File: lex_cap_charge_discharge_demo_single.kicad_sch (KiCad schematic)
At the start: 8 parts, among them J1 +5V, J2 GND, SW1 charge, SW2 discharge

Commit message: Put rev. 1.0 on schematic sheet info box
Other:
- note added: "1.0"
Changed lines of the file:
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@@
 	(generator_version "9.0")
 	(paper "A5")
+	(text "1.0"
+		(exclude_from_sim no)
+		(at 184.404 131.318 0)
+		(effects
+			(font
+				(size 1.524 1.524)
+			)
+		)
+	)
 	(text "momentary"
 		(exclude_from_sim no)

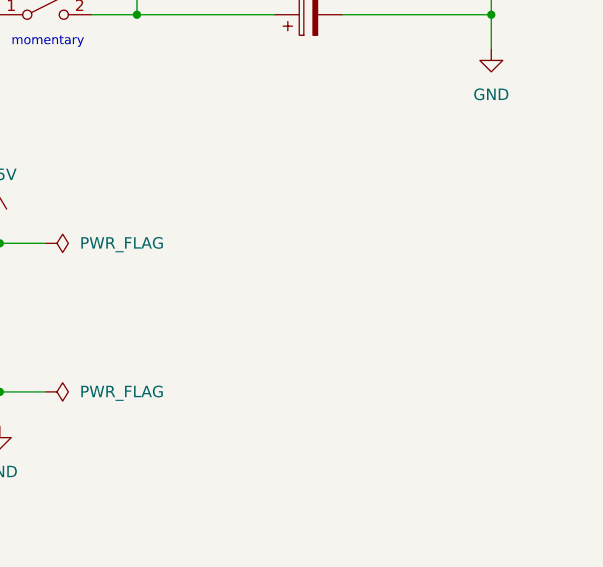
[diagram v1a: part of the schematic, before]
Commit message: Add 2.2mm mounting holes at corners (made board bigger)
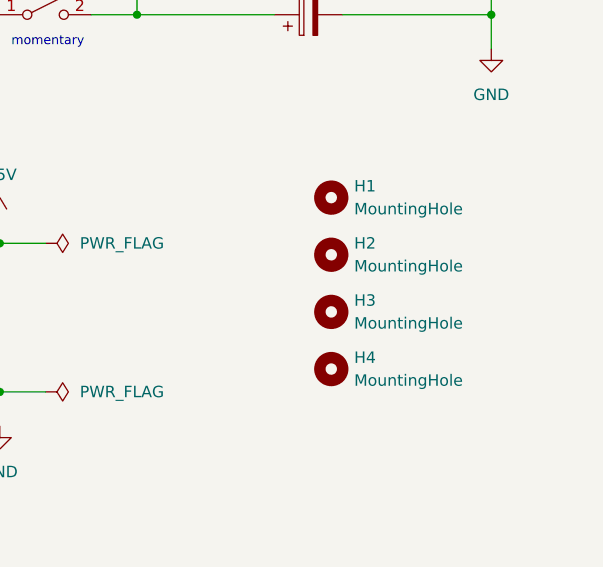
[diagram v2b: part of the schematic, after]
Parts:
- added H1, H2, H3, H4: MountingHole, MountingHole:MountingHole_2.2mm_M2, symbol Mechanical:MountingHole
